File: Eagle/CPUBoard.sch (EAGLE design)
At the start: 33 parts, among them IC2 MAX232, IC3 MAX485CPA, J1 DISPLAY, J2 BUTTON_BOARD, J3 RELAY_BOARD, Q1 12.000MHz, X6 MKDSN1,5/3-5,08, X7 MKDSN1,5/3-5,08

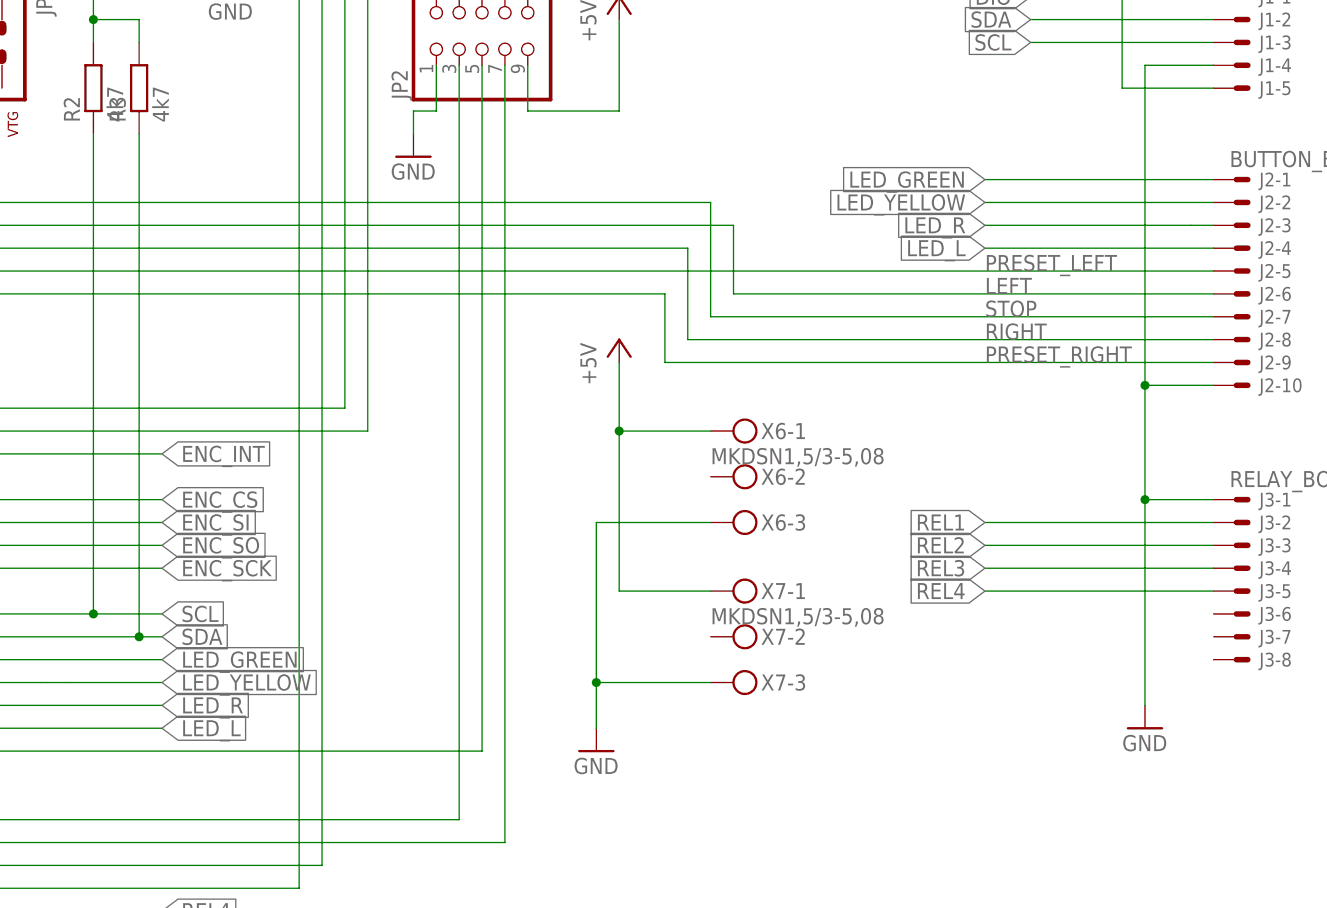
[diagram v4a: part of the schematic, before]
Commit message: - cabling of RelayBoard1 partly changed - some pin-swaps to ButtonBoard -> blrtest.c finally works as expected
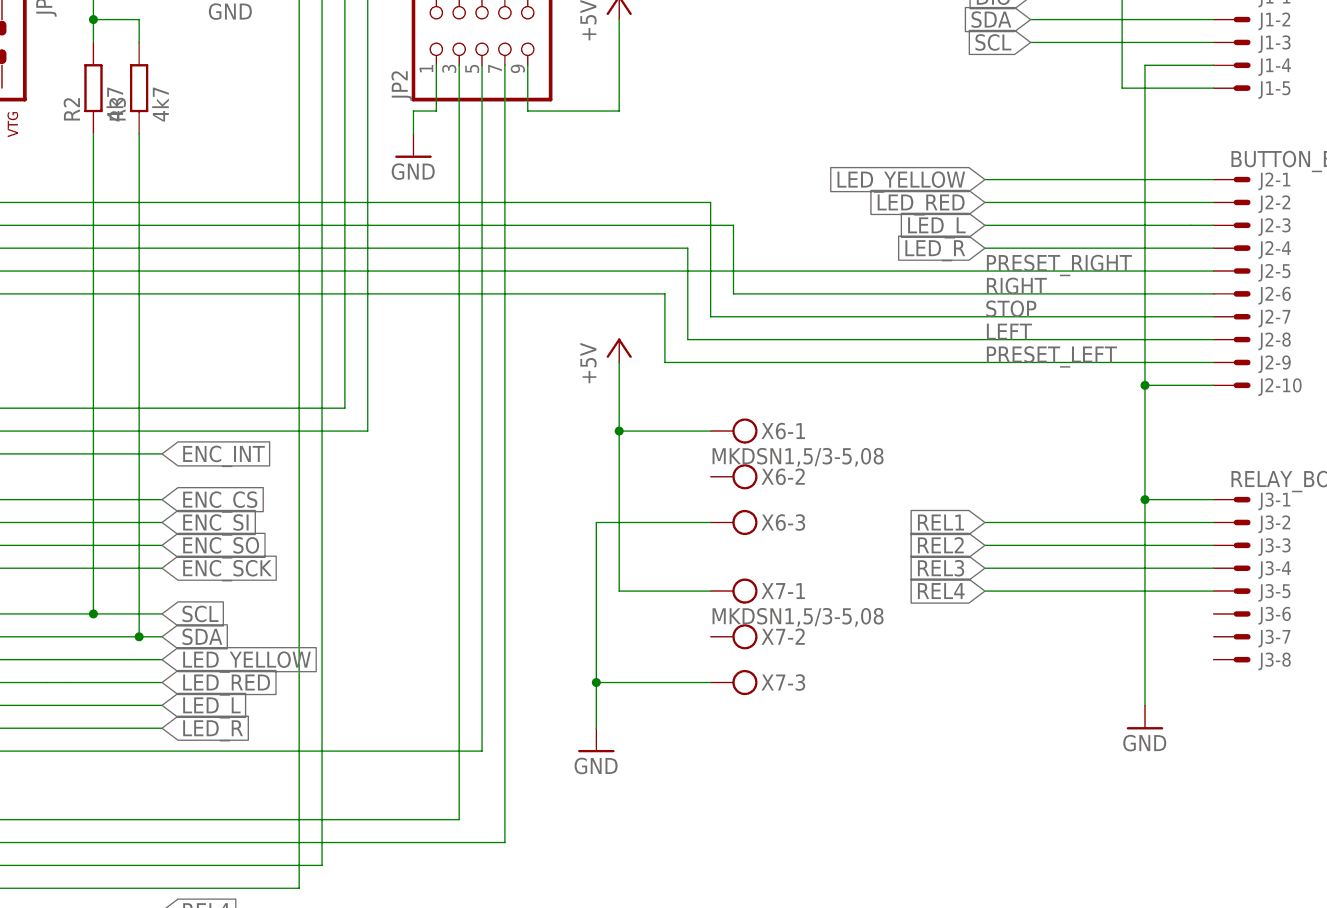
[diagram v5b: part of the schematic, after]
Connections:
- removed net LED_GREEN: IC1.TCK/PCINT18, J2-1.S
- new net LED_RED: IC1.TMS/PCINT19, J2-2.S
- net LED_L: now also IC1.TDO/PCINT20, J2-3.S; no longer IC1.TDI/PCINT21, J2-4.S
- net LED_R: now also IC1.TDI/PCINT21, J2-4.S; no longer IC1.TDO/PCINT20, J2-3.S
- net LED_YELLOW: now also IC1.TCK/PCINT18, J2-1.S; no longer IC1.TMS/PCINT19, J2-2.S
- net LEFT: now also IC1.ADC2/PCINT2, J2-8.S; no longer IC1.ADC1/PCINT1, J2-6.S
- net PRESET_LEFT: now also IC1.ADC4/PCINT4, J2-9.S; no longer IC1.ADC3/PCINT3, J2-5.S
- net PRESET_RIGHT: now also IC1.ADC3/PCINT3, J2-5.S; no longer IC1.ADC4/PCINT4, J2-9.S
- net RIGHT: now also IC1.ADC1/PCINT1, J2-6.S; no longer IC1.ADC2/PCINT2, J2-8.S
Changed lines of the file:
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@@
 </segment>
 </net>
-<net name="LED_GREEN" class="0">
-<segment>
-<wire x1="241.3" y1="104.14" x2="215.9" y2="104.14" width="0.1524" layer="91"/>
-<label x="215.9" y="104.14" size="1.778" layer="95" rot="MR0" xref="yes"/>
-<pinref part="J2" gate="-1" pin="S"/>
-</segment>
-<segment>
-<wire x1="91.44" y1="50.8" x2="124.46" y2="50.8" width="0.1524" layer="91"/>
-<label x="124.46" y="50.8" size="1.778" layer="95" xref="yes"/>
-<pinref part="IC1" gate="G$1" pin="TCK/PCINT18"/>
-</segment>
-</net>
-<net name="LED_YELLOW" class="0">
-<segment>
-<label x="215.9" y="101.6" size="1.778" layer="95" rot="MR0" xref="yes"/>
-<pinref part="J2" gate="-2" pin="S"/>
-<wire x1="241.3" y1="101.6" x2="215.9" y2="101.6" width="0.1524" layer="91"/>
-</segment>
-<segment>
-<wire x1="111.76" y1="48.26" x2="114.3" y2="48.26" width="0.1524" layer="91"/>
-<label x="124.46" y="48.26" size="1.778" layer="95" xref="yes"/>
-<pinref part="IC1" gate="G$1" pin="TMS/PCINT19"/>
-<wire x1="114.3" y1="48.26" x2="124.46" y2="48.26" width="0.1524" layer="91"/>
-<wire x1="91.44" y1="48.26" x2="111.76" y2="48.26" width="0.1524" layer="91"/>
-</segment>
-</net>
-<net name="LED_L" class="0">
-<segment>
-<label x="124.46" y="43.18" size="1.778" layer="95" xref="yes"/>
-<pinref part="IC1" gate="G$1" pin="TDI/PCINT21"/>
-<wire x1="91.44" y1="43.18" x2="124.46" y2="43.18" width="0.1524" layer="91"/>
-</segment>
-<segment>
-<wire x1="241.3" y1="96.52" x2="215.9" y2="96.52" width="0.1524" layer="91"/>
-<label x="215.9" y="96.52" size="1.778" layer="95" rot="MR0" xref="yes"/>
-<pinref part="J2" gate="-4" pin="S"/>
-</segment>
-</net>
-<net name="LED_R" class="0">
-<segment>
-<wire x1="91.44" y1="45.72" x2="124.46" y2="45.72" width="0.1524" layer="91"/>
-<label x="124.46" y="45.72" size="1.778" layer="95" xref="yes"/>
-<pinref part="IC1" gate="G$1" pin="TDO/PCINT20"/>
-</segment>
-<segment>
-<wire x1="241.3" y1="99.06" x2="238.76" y2="99.06" width="0.1524" layer="91"/>
-<label x="215.9" y="99.06" size="1.778" layer="95" rot="MR0" xref="yes"/>
-<pinref part="J2" gate="-3" pin="S"/>
-<wire x1="238.76" y1="99.06" x2="215.9" y2="99.06" width="0.1524" layer="91"/>
-</segment>
-</net>
-<net name="PRESET_LEFT" class="0">
+<net name="PRESET_RIGHT" class="0">
 <segment>
 <label x="215.9" y="93.98" size="1.778" layer="95"/>
@@
 </segment>
 </net>
-<net name="LEFT" class="0">
+<net name="RIGHT" class="0">
 <segment>
 <wire x1="241.3" y1="91.44" x2="187.96" y2="91.44" width="0.1524" layer="91"/>
@@
 </segment>
 </net>
-<net name="RIGHT" class="0">
+<net name="LEFT" class="0">
 <segment>
 <wire x1="241.3" y1="86.36" x2="182.88" y2="86.36" width="0.1524" layer="91"/>
@@
 </segment>
 </net>
-<net name="PRESET_RIGHT" class="0">
+<net name="PRESET_LEFT" class="0">
 <segment>
 <label x="215.9" y="83.82" size="1.778" layer="95"/>
@@
 </segment>
 </net>
+<net name="LED_R" class="0">
+<segment>
+<wire x1="241.3" y1="96.52" x2="215.9" y2="96.52" width="0.1524" layer="91"/>
+<label x="215.9" y="96.52" size="1.778" layer="95" rot="MR0" xref="yes"/>
+<pinref part="J2" gate="-4" pin="S"/>
+</segment>
+<segment>
+<label x="124.46" y="43.18" size="1.778" layer="95" xref="yes"/>
+<pinref part="IC1" gate="G$1" pin="TDI/PCINT21"/>
+<wire x1="91.44" y1="43.18" x2="124.46" y2="43.18" width="0.1524" layer="91"/>
+</segment>
+</net>
+<net name="LED_L" class="0">
+<segment>
+<wire x1="91.44" y1="45.72" x2="124.46" y2="45.72" width="0.1524" layer="91"/>
+<label x="124.46" y="45.72" size="1.778" layer="95" xref="yes"/>
+<pinref part="IC1" gate="G$1" pin="TDO/PCINT20"/>
+</segment>
+<segment>
+<wire x1="241.3" y1="99.06" x2="238.76" y2="99.06" width="0.1524" layer="91"/>
+<label x="215.9" y="99.06" size="1.778" layer="95" rot="MR0" xref="yes"/>
+<pinref part="J2" gate="-3" pin="S"/>
+<wire x1="238.76" y1="99.06" x2="215.9" y2="99.06" width="0.1524" layer="91"/>
+</segment>
+</net>
+<net name="LED_RED" class="0">
+<segment>
+<wire x1="111.76" y1="48.26" x2="114.3" y2="48.26" width="0.1524" layer="91"/>
+<label x="124.46" y="48.26" size="1.778" layer="95" xref="yes"/>
+<pinref part="IC1" gate="G$1" pin="TMS/PCINT19"/>
+<wire x1="114.3" y1="48.26" x2="124.46" y2="48.26" width="0.1524" layer="91"/>
+<wire x1="91.44" y1="48.26" x2="111.76" y2="48.26" width="0.1524" layer="91"/>
+</segment>
+<segment>
+<label x="215.9" y="101.6" size="1.778" layer="95" rot="MR0" xref="yes"/>
+<pinref part="J2" gate="-2" pin="S"/>
+<wire x1="241.3" y1="101.6" x2="215.9" y2="101.6" width="0.1524" layer="91"/>
+</segment>
+</net>
+<net name="LED_YELLOW" class="0">
+<segment>
+<wire x1="91.44" y1="50.8" x2="124.46" y2="50.8" width="0.1524" layer="91"/>
+<label x="124.46" y="50.8" size="1.778" layer="95" xref="yes"/>
+<pinref part="IC1" gate="G$1" pin="TCK/PCINT18"/>
+</segment>
+<segment>
+<wire x1="241.3" y1="104.14" x2="215.9" y2="104.14" width="0.1524" layer="91"/>
+<label x="215.9" y="104.14" size="1.778" layer="95" rot="MR0" xref="yes"/>
+<pinref part="J2" gate="-1" pin="S"/>
+</segment>
+</net>
